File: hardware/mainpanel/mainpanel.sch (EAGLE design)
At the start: 15 parts, among them J1 CDH, J2 OW, J3 DBG, J4 SUN-UART, J5 SUN, J6 ENV, J7 ADCS, U1 DS18B20, U2 DS18B20

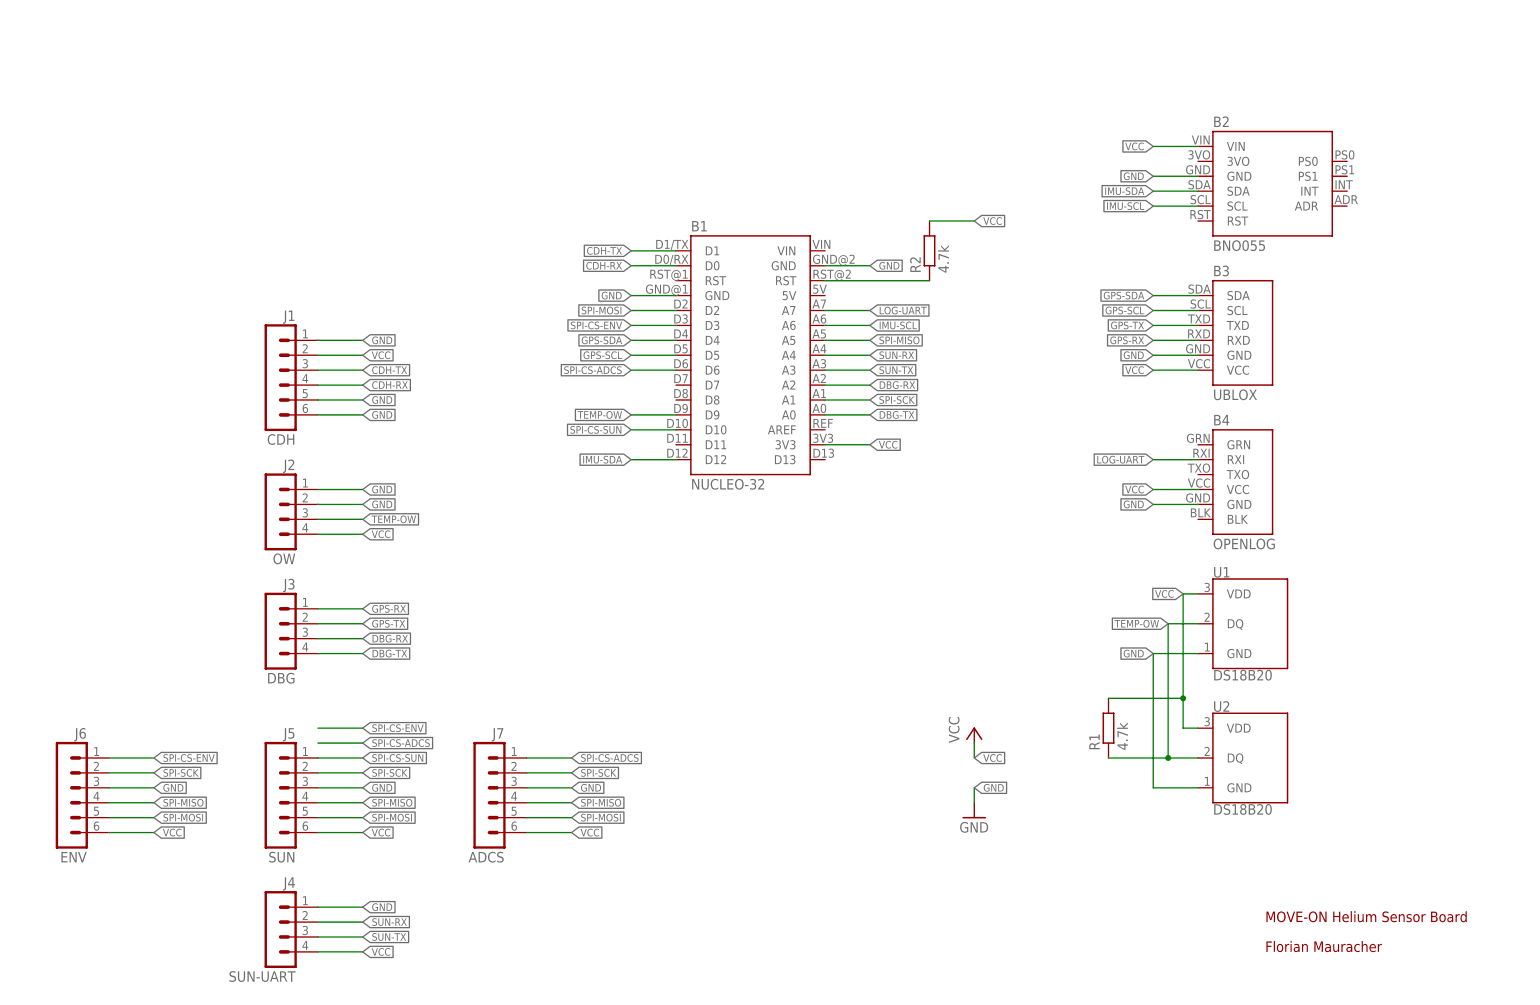
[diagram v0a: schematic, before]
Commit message: Move components and add 3rd DS18B20
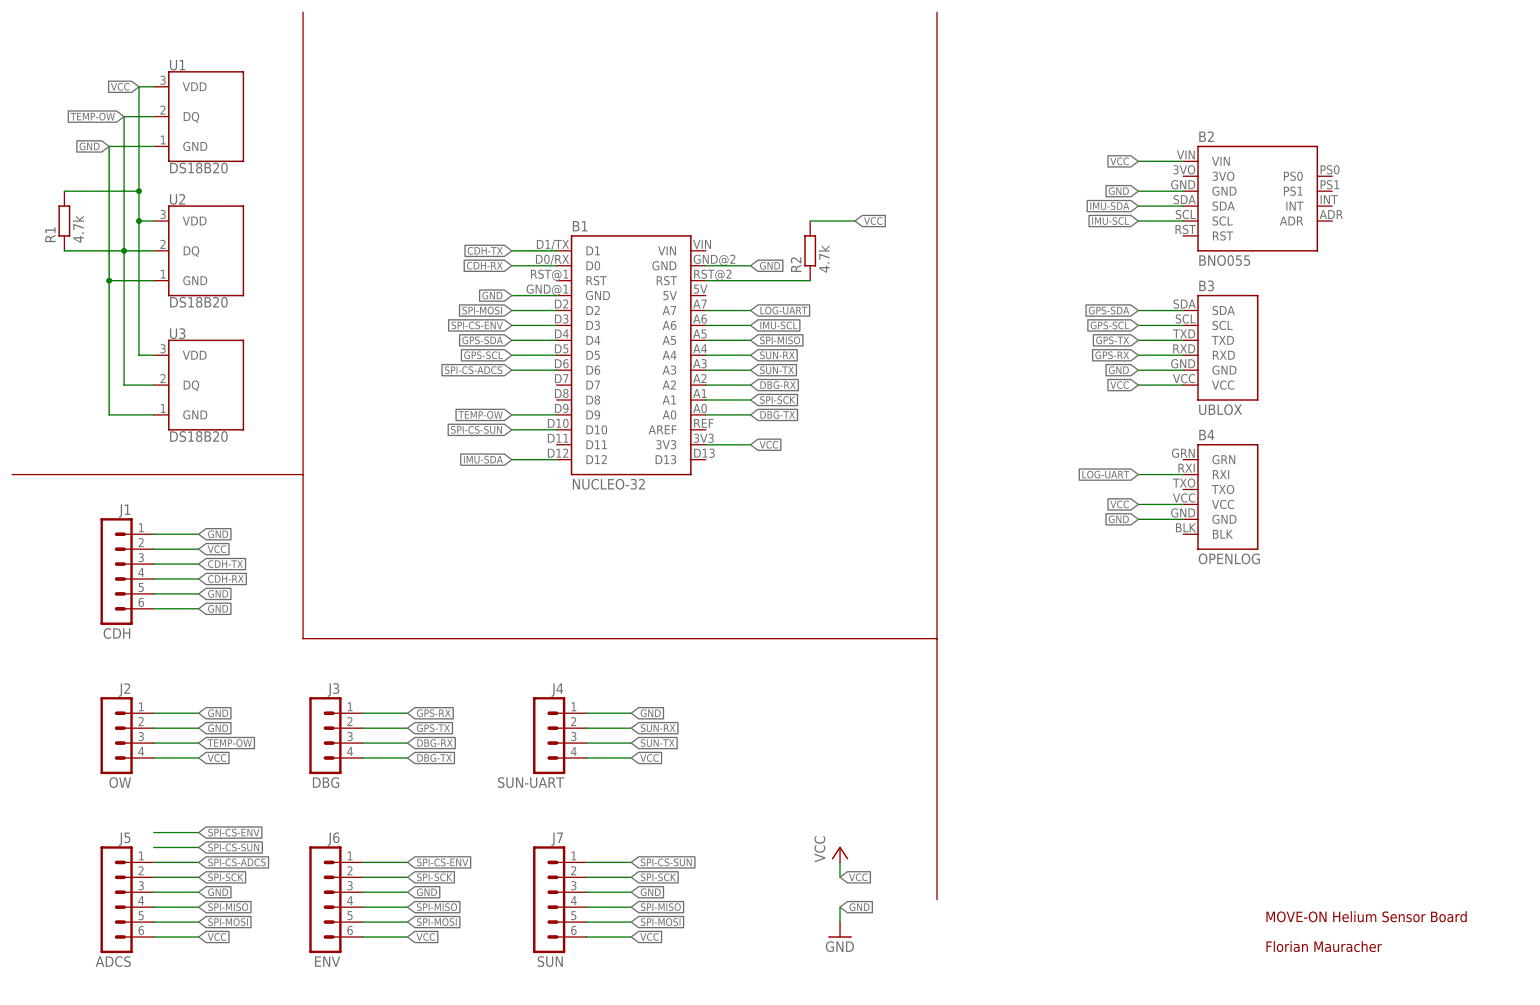
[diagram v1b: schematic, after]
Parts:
- added U3: DS18B20, Frcy:DS18B20
- J5: value SUN -> ADCS
- J7: value ADCS -> SUN
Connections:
- net GND: now also U3.GND
- net SPI-CS-ADCS: now also J5.1; no longer J7.1
- net SPI-CS-SUN: now also J7.1; no longer J5.1
- net TEMP-OW: now also U3.DQ
- net VCC: now also U3.VDD
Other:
- moved on the sheet: B1, B2, B3, B4, J1, J2, J3, J4, J5, J6, J7, R1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

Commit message: Move stuff
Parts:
- added R3, R4, R5, R6: 4.7k, resistor:R-EU_M2012
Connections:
- net GPS-SCL: now also R5.2
- net GPS-SDA: now also R6.2
- net IMU-SCL: now also R3.2
- net IMU-SDA: now also R4.2
- net N$1: now also R2.2; no longer R2.1
- net VCC: now also R2.1, R3.1, R4.1, R5.1, R6.1; no longer R2.2
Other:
- moved on the sheet: B2, B3, B4, R2

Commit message: Use rcl lib for resistors
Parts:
- R1, R2, R3, R4, R5, R6: device resistor:R-EU_M2012 -> rcl:R-EU_R2012
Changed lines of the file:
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@@
 <setting verticaltext="up"/>
 </settings>
-<grid distance="0.1" unitdist="inch" unit="inch" style="lines" multiple="1" display="yes" altdistance="0.05" altunitdist="inch" altunit="inch"/>
+<grid distance="0.1" unitdist="inch" unit="inch" style="lines" multiple="1" display="no" altdistance="0.01" altunitdist="inch" altunit="inch"/>
 <layers>
 <layer number="1" name="Top" color="4" fill="1" visible="no" active="no"/>
@@
 <part name="J3" library="con-molex-c-grid" deviceset="90136-1?04" device="" value="DBG"/>
 <part name="J1" library="con-molex-c-grid" deviceset="90136-1?06" device="" value="CDH"/>
-<part name="R1" library="resistor" library_urn="urn:adsk.eagle:library:348" deviceset="R-EU_" device="M2012" package3d_urn="urn:adsk.eagle:package:26082/1" value="4.7k"/>
+<part name="R1" library="rcl" library_urn="urn:adsk.eagle:library:334" deviceset="R-EU_" device="R2012" package3d_urn="urn:adsk.eagle:package:23543/2" value="4.7k"/>
 <part name="U1" library="Frcy" deviceset="DS18B20" device=""/>
 <part name="U2" library="Frcy" deviceset="DS18B20" device=""/>
-<part name="R2" library="resistor" library_urn="urn:adsk.eagle:library:348" deviceset="R-EU_" device="M2012" package3d_urn="urn:adsk.eagle:package:26082/1" value="4.7k"/>
+<part name="R2" library="rcl" library_urn="urn:adsk.eagle:library:334" deviceset="R-EU_" device="R2012" package3d_urn="urn:adsk.eagle:package:23543/2" value="4.7k"/>
 <part name="J6" library="con-molex-c-grid" deviceset="90136-1?06" device="" value="ENV"/>
 <part name="J4" library="con-molex-c-grid" deviceset="90136-1?04" device="" value="SUN-UART"/>
@@
 <part name="FRAME1" library="frames" library_urn="urn:adsk.eagle:library:229" deviceset="A4L-LOC" device=""/>
 <part name="U3" library="Frcy" deviceset="DS18B20" device=""/>
-<part name="R3" library="resistor" library_urn="urn:adsk.eagle:library:348" deviceset="R-EU_" device="M2012" package3d_urn="urn:adsk.eagle:package:26082/1" value="4.7k"/>
-<part name="R4" library="resistor" library_urn="urn:adsk.eagle:library:348" deviceset="R-EU_" device="M2012" package3d_urn="urn:adsk.eagle:package:26082/1" value="4.7k"/>
-<part name="R5" library="resistor" library_urn="urn:adsk.eagle:library:348" deviceset="R-EU_" device="M2012" package3d_urn="urn:adsk.eagle:package:26082/1" value="4.7k"/>
-<part name="R6" library="resistor" library_urn="urn:adsk.eagle:library:348" deviceset="R-EU_" device="M2012" package3d_urn="urn:adsk.eagle:package:26082/1" value="4.7k"/>
+<part name="R3" library="rcl" library_urn="urn:adsk.eagle:library:334" deviceset="R-EU_" device="R2012" package3d_urn="urn:adsk.eagle:package:23543/2" value="4.7k"/>
+<part name="R4" library="rcl" library_urn="urn:adsk.eagle:library:334" deviceset="R-EU_" device="R2012" package3d_urn="urn:adsk.eagle:package:23543/2" value="4.7k"/>
+<part name="R5" library="rcl" library_urn="urn:adsk.eagle:library:334" deviceset="R-EU_" device="R2012" package3d_urn="urn:adsk.eagle:package:23543/2" value="4.7k"/>
+<part name="R6" library="rcl" library_urn="urn:adsk.eagle:library:334" deviceset="R-EU_" device="R2012" package3d_urn="urn:adsk.eagle:package:23543/2" value="4.7k"/>
 </parts>
 <sheets>
@@
 packages will not be understood (or retained) with this version.
 </note>
+<note version="8.4" severity="warning">
+Since Version 8.4, EAGLE supports properties for SPICE simulation.
+Probes in schematics and SPICE mapping objects found in parts and library devices
+will not be understood with this version. Update EAGLE to the latest version
+for full support of SPICE simulation.
+</note>
 </compatibility>

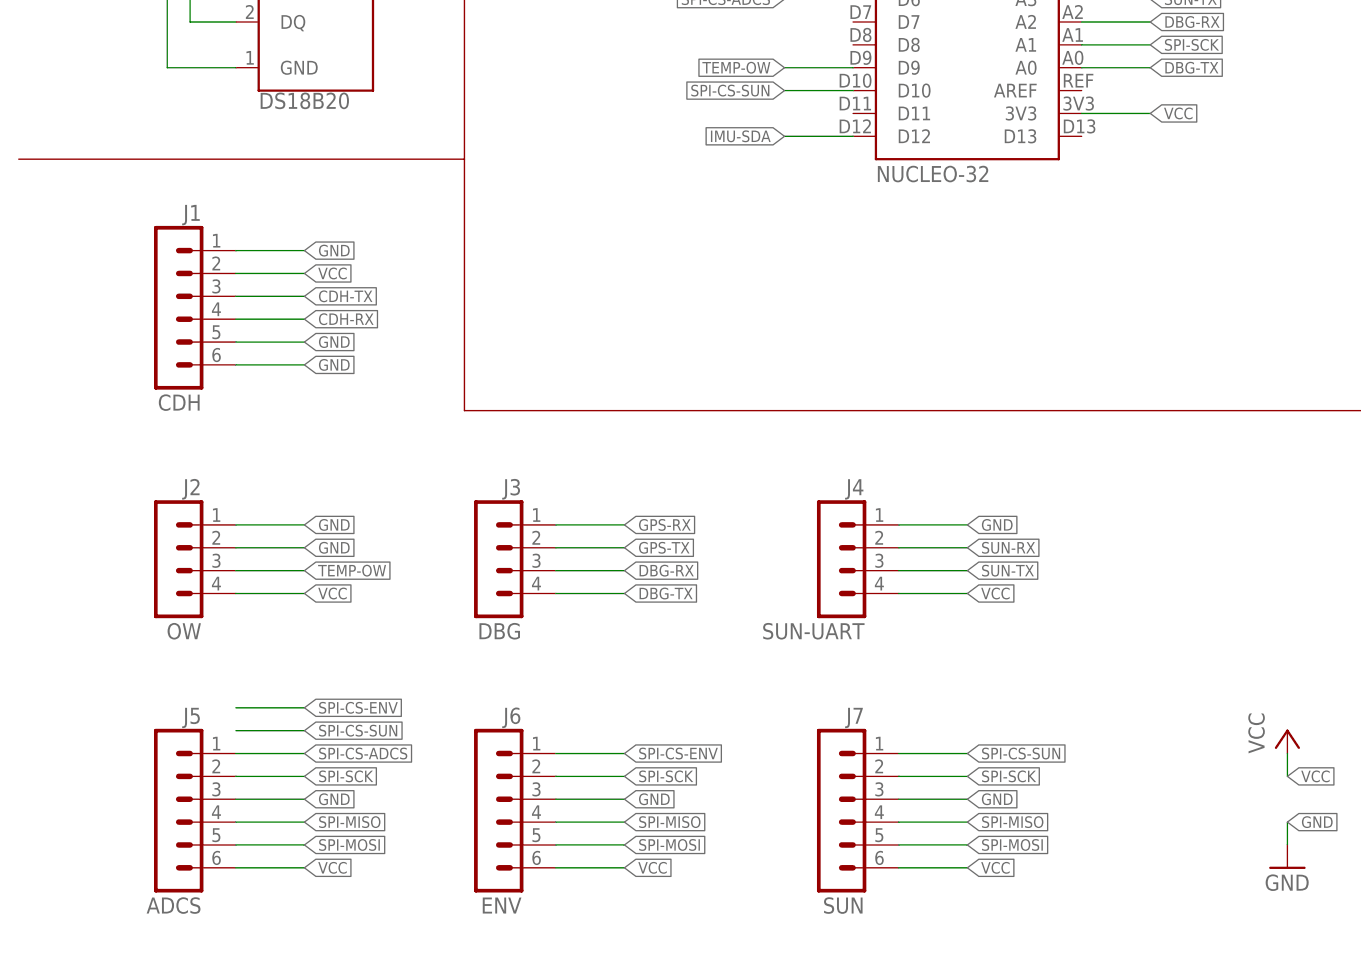
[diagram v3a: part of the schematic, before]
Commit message: Use 0.1uF caps on all vcc/gnd lines
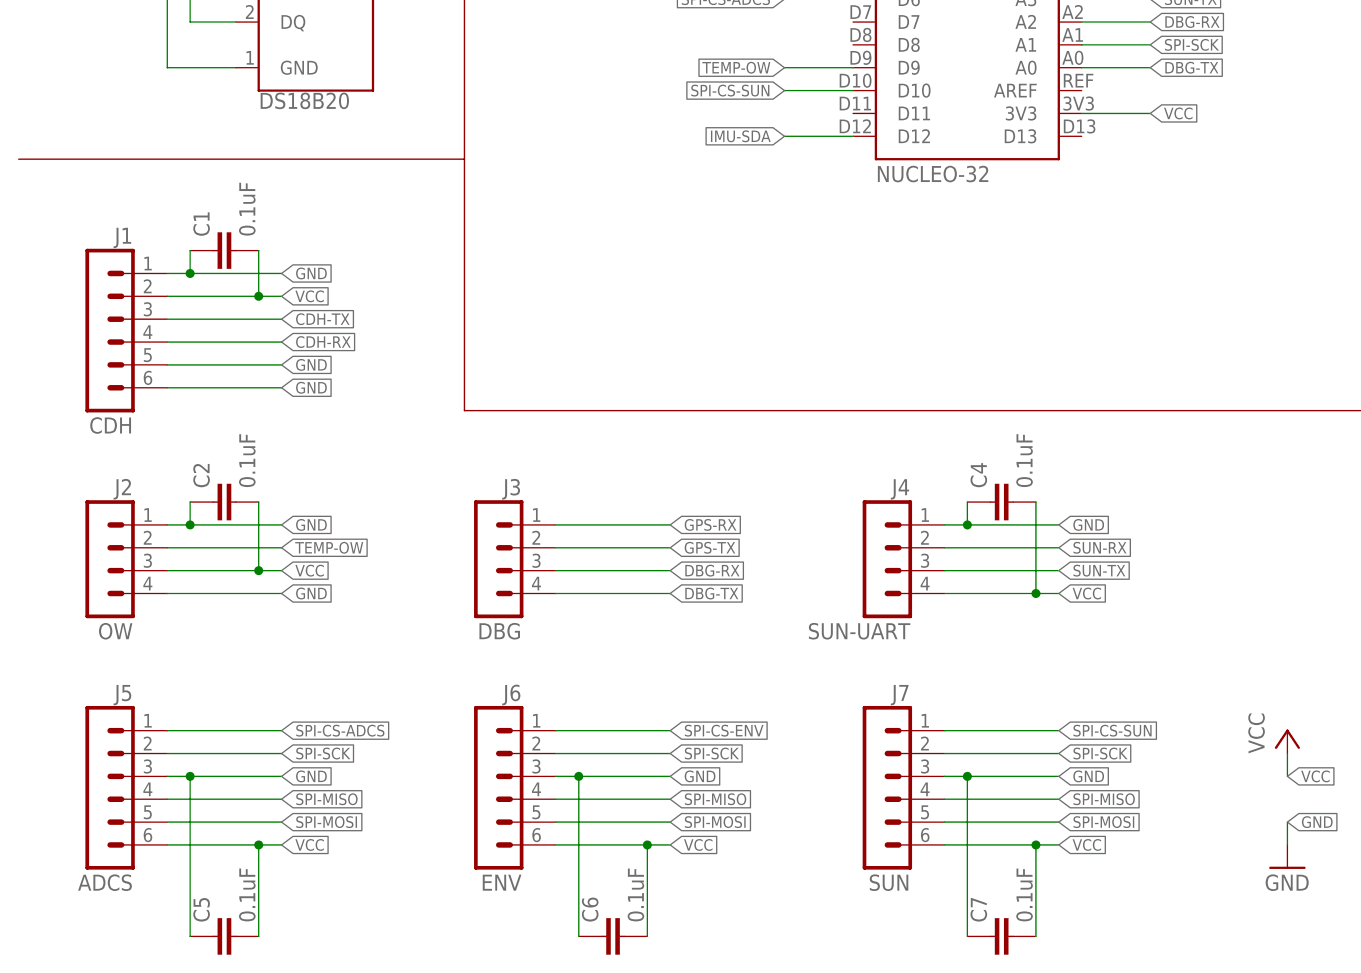
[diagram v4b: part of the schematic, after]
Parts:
- added C1, C2, C4, C5, C6, C7: 0.1uF, rcl:C-EUC2012
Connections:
- net GND: now also C1.1, C2.1, C4.1, C5.1, C6.1, C7.1, J2.4; no longer J2.2
- net TEMP-OW: now also J2.2; no longer J2.3
- net VCC: now also C1.2, C2.2, C4.2, C5.2, C6.2, C7.2, J2.3; no longer J2.4
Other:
- moved on the sheet: J1, J2, J4, J5, J6, J7

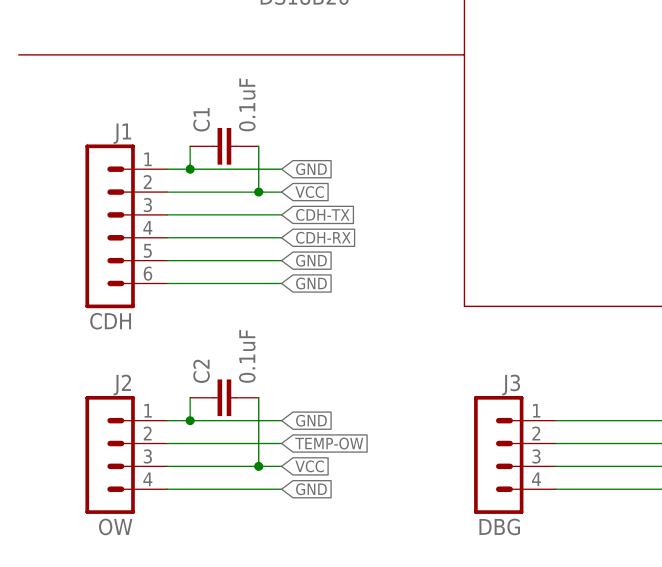
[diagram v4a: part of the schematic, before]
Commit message: Disconnect pin 6 to cdh
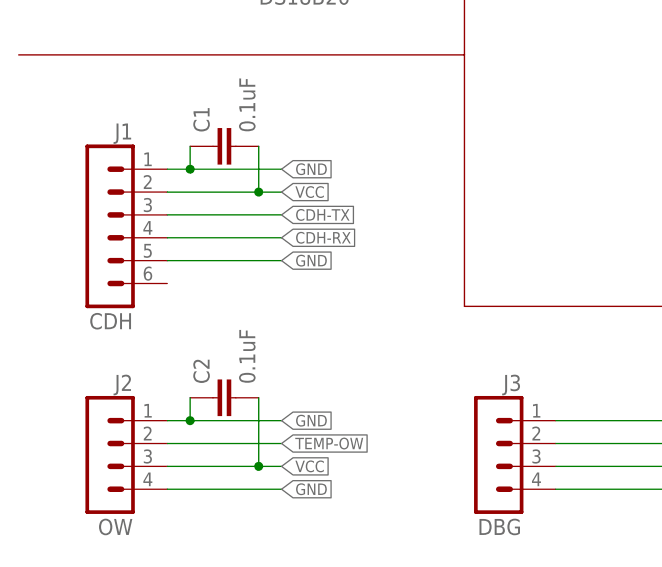
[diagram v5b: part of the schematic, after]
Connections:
- net GND: no longer J1.6
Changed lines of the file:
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@@
-</segment>
-<segment>
-<pinref part="J1" gate="G$1" pin="6"/>
-<wire x1="20.32" y1="71.12" x2="33.02" y2="71.12" width="0.1524" layer="91"/>
-<label x="33.02" y="71.12" size="1.27" layer="95" xref="yes"/>
 </segment>
 <segment>
